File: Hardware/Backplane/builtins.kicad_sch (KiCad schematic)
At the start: 40 parts, among them J1001 Conn_01x06, J1002 Conn_01x06, J1003 Conn_01x06, J1004 Conn_01x06, Q1002 S3134K, Q1004 S3134K, Q1005 S3134K, SW1001 SW_Push, U1003 CD74HC221M96, U1004 PCF8523T/1,118, Y1001 32.768k

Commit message: Adjusts to review comments
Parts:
- removed J1001, J1002, J1003, J1004: Conn_01x06, Connector_PinHeader_2.54mm:PinHeader_1x06_P2.54mm_Vertical, symbol Connector_Generic:Conn_01x06
- removed TP1001, TP1002, TP1003: TestPoint_Small, TestPoint:TestPoint_Pad_D1.0mm, symbol Connector:TestPoint_Small
- added J1001, J1002, J1003, J1005: SM04B-SRSS-TB, symbol Connector_Generic:Conn_01x04
- added R1004, R1006, R1011: 270, Resistor_SMD:R_0603_1608Metric, symbol Device:R
- C1003, C1004: value 1u -> 10u; Digikey Part No (none) -> 1276-1192-1-ND
- R1001, R1002: value 4K7 -> 10K; Digikey Part No (none) -> 311-10.0KHRCT-ND
- R1003, R1009, R1010, R1013, R1016: Digikey Part No (none) -> 311-10.0KHRCT-ND
- R1005, R1007, R1008: footprint (none) -> Resistor_SMD:R_0603_1608Metric; Digikey Part No (none) -> 541-100HCT-ND
- R1014, R1015: value 100K -> 10K; Digikey Part No (none) -> 311-10.0KHRCT-ND
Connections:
- net +3V3: now also R1013.1, J1001.3 (Pin_3), J1002.3 (Pin_3), J1003.3 (Pin_3), J1005.3 (Pin_3)
- net BRD_RESET: now also R1004.2; no longer Q1002.2 (G)
- net GND: now also J1001.4 (Pin_4), J1002.4 (Pin_4), J1003.4 (Pin_4), J1005.4 (Pin_4); no longer R1013.1
- net I2C^{BRD}_{SCL}: now also J1001.1 (Pin_1), J1002.1 (Pin_1), J1003.1 (Pin_1), J1005.1 (Pin_1)
- net I2C^{BRD}_{SDA}: now also J1001.2 (Pin_2), J1002.2 (Pin_2), J1003.2 (Pin_2), J1005.2 (Pin_2)
- net at Q1005.2 (G): now also R1006.1; no longer U1003.13 (1Q)
- net at Q1004.2 (G): now also R1011.1; no longer U1003.5 (2Q)
- new net: Q1002.2 (G), R1004.1
- new net: R1011.2, U1003.5 (2Q)
- new net: R1006.2, U1003.13 (1Q)
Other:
- note removed: "TODO: Change to QWIIC"
- moved on the sheet: Q1005

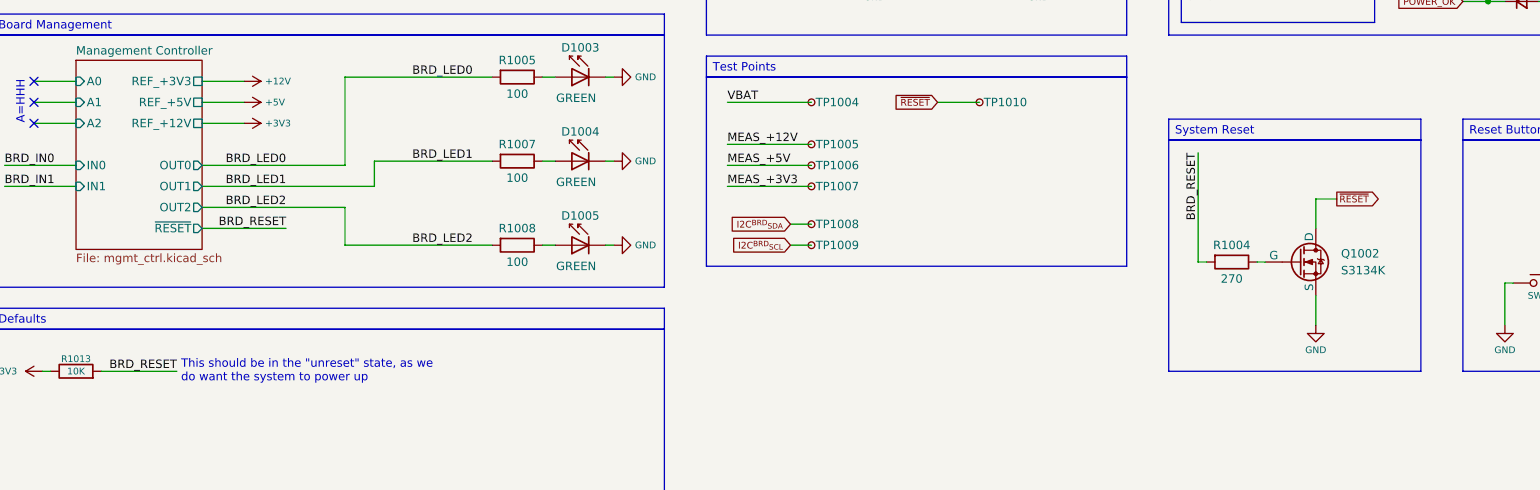
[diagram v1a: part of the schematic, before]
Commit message: Starts refactoring Backplane to use NL17SZS11-D instead of 4-port AND
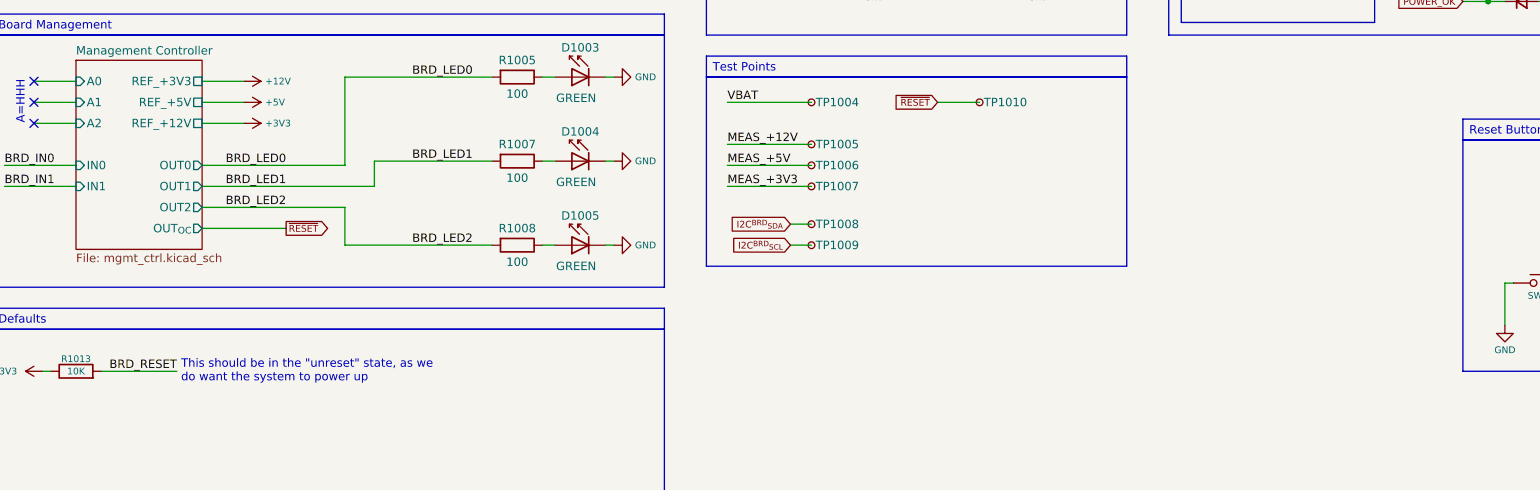
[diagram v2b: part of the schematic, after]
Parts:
- removed Q1002: S3134K, symbol Simulation_SPICE:NMOS
- removed R1004: 270, Resistor_SMD:R_0603_1608Metric, symbol Device:R
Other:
- sheet Management Controller ports: added OUT_{OC}; removed ~{RESET}

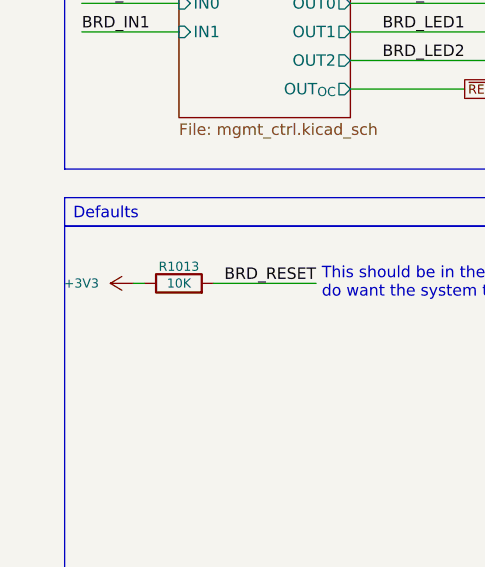
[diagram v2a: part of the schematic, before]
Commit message: Cleans up Backplane schematic even more. Less parts in the BOM, less mistakes!
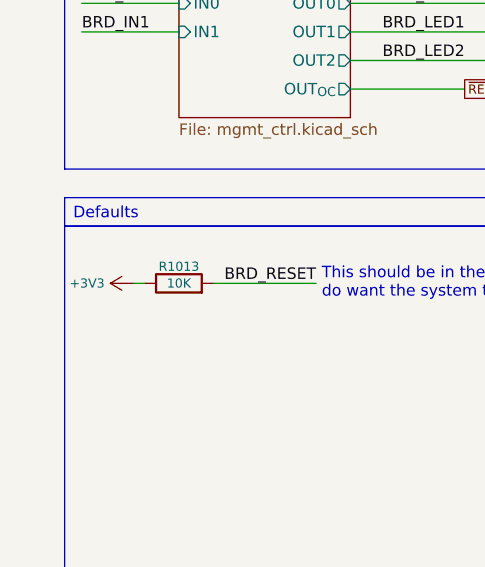
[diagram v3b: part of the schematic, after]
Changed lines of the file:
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@@
 		(on_board yes)
 		(dnp no)
-		(fields_autoplaced yes)
 		(property "Reference" "#PWR01004"
 			(at 30.48 158.75 0)
@@
 		)
 		(property "Value" "+3V3"
-			(at 22.86 158.7499 90)
+			(at 23.495 158.75 90)
 			(effects
 				(font

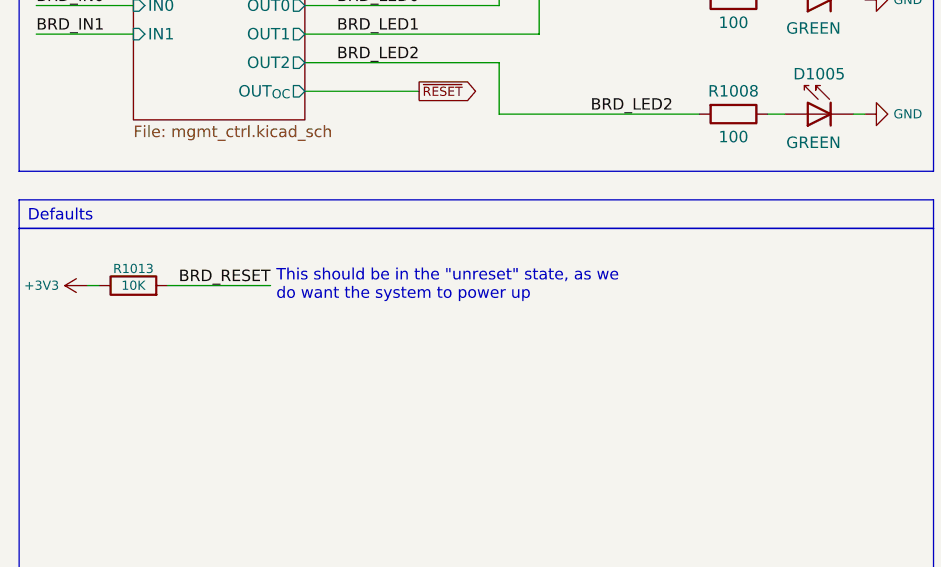
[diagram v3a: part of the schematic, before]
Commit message: Cleans up power connector.
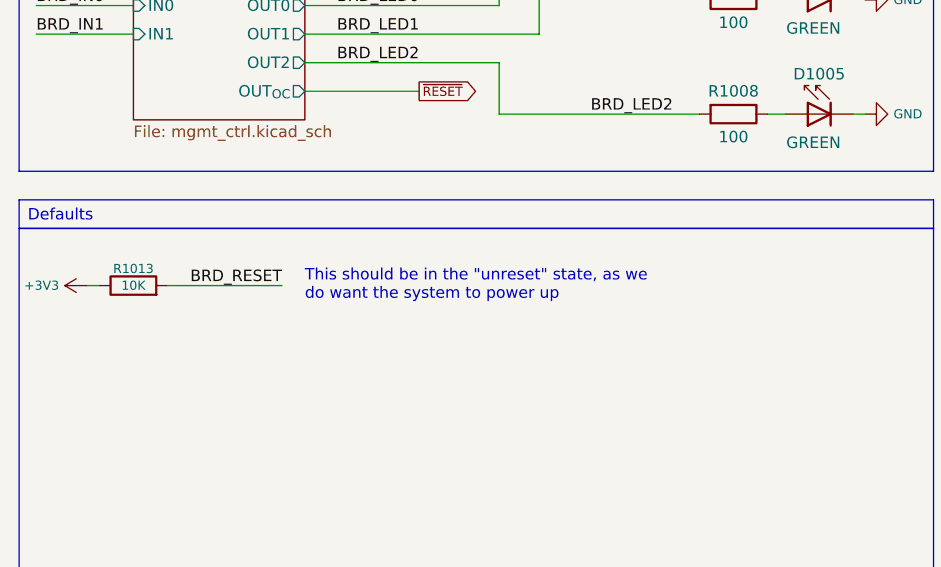
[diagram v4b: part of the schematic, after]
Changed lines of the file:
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@@
 	(text "This should be in the \"unreset\" state, as we\ndo want the system to power up"
 		(exclude_from_sim no)
-		(at 47.625 158.75 0)
+		(at 50.8 158.75 0)
 		(effects
 			(font
@@
 	(wire
 		(pts
-			(xy 35.56 158.75) (xy 46.99 158.75)
+			(xy 35.56 158.75) (xy 48.26 158.75)
 		)
 		(stroke
@@
 	)
 	(label "BRD_RESET"
-		(at 46.99 158.75 180)
-		(effects
-			(font
+		(at 48.26 158.75 180)
+		(effects
+			(font

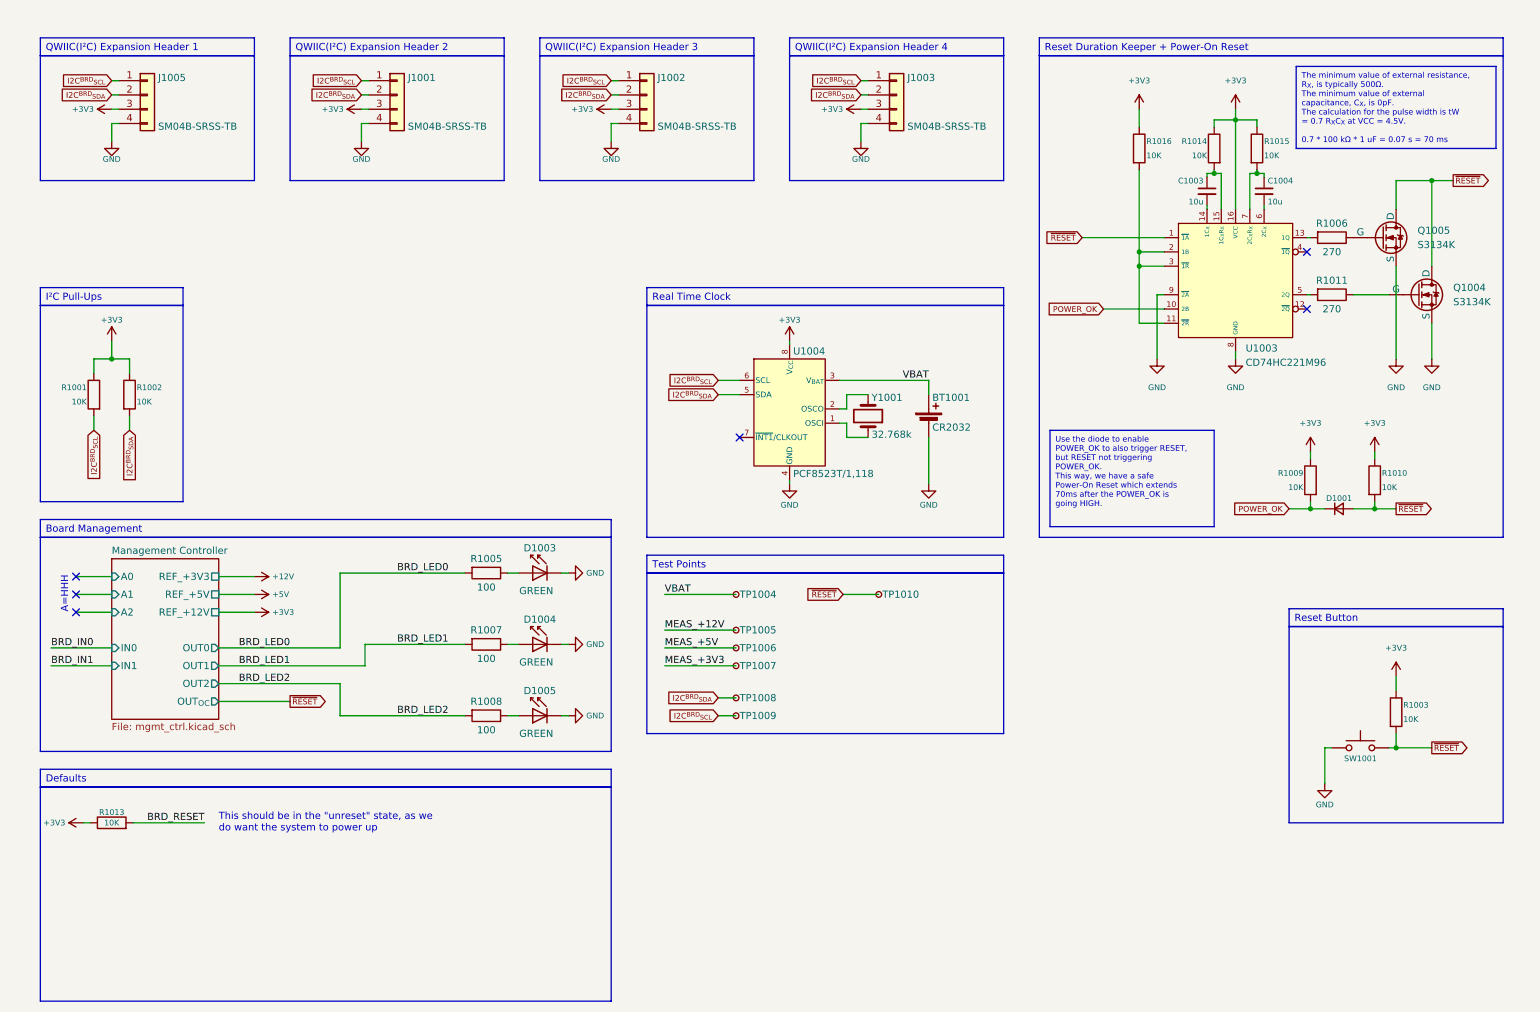
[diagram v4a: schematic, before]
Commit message: Cleans up schematic even more, consolidates 270 and 100 Ohm resistors into the 560 ohm resistor, as they were only used as series resistors for the mosfets and LED current limiters
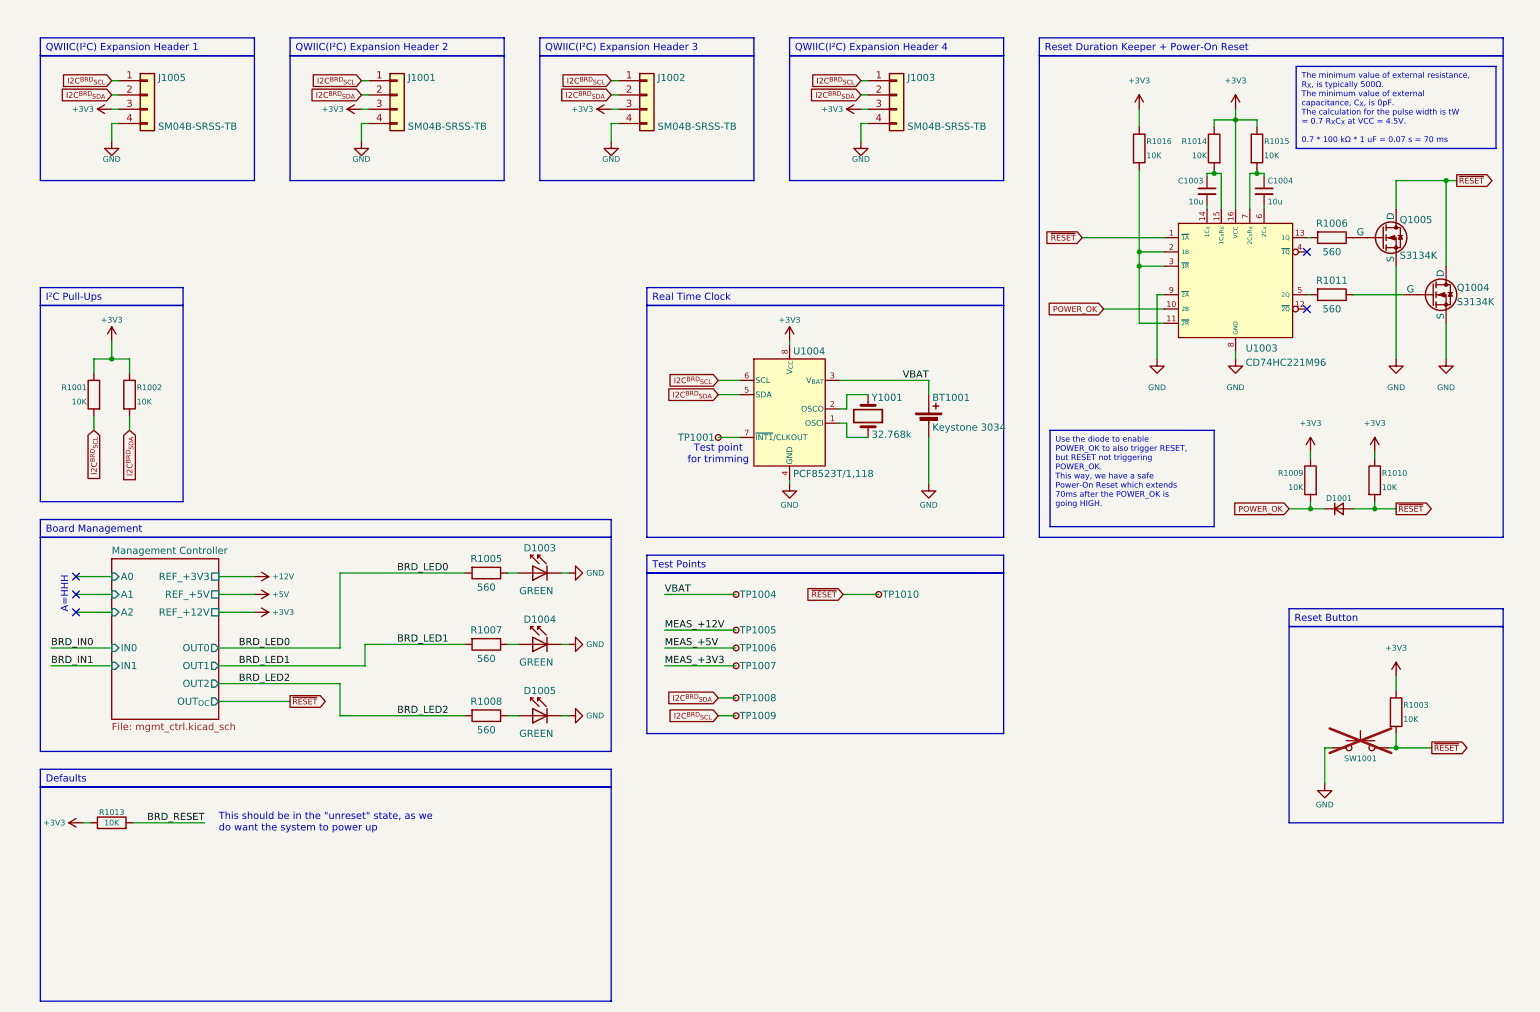
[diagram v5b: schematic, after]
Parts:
- added TP1001: TestPoint_Small, TestPoint:TestPoint_Pad_D1.0mm, symbol Connector:TestPoint_Small
- BT1001: value CR2032 -> Keystone 3034; footprint Battery:Battery_Panasonic_CR2032-HFN_Horizontal_CircularHoles -> Battery:BatteryHolder_Keystone_3034_1x20mm; Digikey Part No (none) -> 36-3034-ND
- Q1004, Q1005: footprint (none) -> Package_TO_SOT_SMD:SOT-23; symbol Simulation_SPICE:NMOS -> Home Computer:S3134K
- R1005, R1007, R1008: value 100 -> 560; Digikey Part No 541-100HCT-ND -> RR08P560DCT-ND
- R1006, R1011: value 270 -> 560; Digikey Part No RMCF0603FT270RCT-ND -> RR08P560DCT-ND
- SW1001: value SW_Push -> Button 12mm; footprint (none) -> Button_Switch_THT:SW_PUSH-12mm; now not fitted
- U1003: footprint (none) -> Package_SO:SOIC-16_3.9x9.9mm_P1.27mm
- Y1001: footprint (none) -> Crystal:Crystal_SMD_3215-2Pin_3.2x1.5mm; Digikey Part No (none) -> 3155-32.768K12.5PI/3215ACT-ND
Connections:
- net GND: now also Q1004.2 (S), Q1005.2 (S); no longer Q1004.3 (S), Q1005.3 (S)
- net ~{RESET}: now also Q1004.3 (D), Q1005.3 (D); no longer Q1004.1 (D), Q1005.1 (D)
- net at R1011.1: now also Q1004.1 (G); no longer Q1004.2 (G)
- net at R1006.1: now also Q1005.1 (G); no longer Q1005.2 (G)
- net at U1004.7 (~{INT1}/CLKOUT): now also TP1001.1
- no-connect marks 6 -> 5
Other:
- note added: "Test point for trimming"
- moved on the sheet: Q1004

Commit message: Further backplane PCB cleanup.
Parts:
- removed J1001, J1002: SM04B-SRSS-TB, symbol Connector_Generic:Conn_01x04
- added J1004, J1006: BM04B-SRSS-TB, Connector_JST:JST_SH_BM04B-SRSS-TB_1x04-1MP_P1.00mm_Vertical, symbol Connector_Generic:Conn_01x04
- J1003, J1005: value SM04B-SRSS-TB -> BM04B-SRSS-TB; footprint (none) -> Connector_JST:JST_SH_BM04B-SRSS-TB_1x04-1MP_P1.00mm_Vertical; Digikey Part No 455-SM04B-SRSS-TBCT-ND -> 455-BM04B-SRSS-TBCT-ND; now not fitted; now left out of the parts list
- SW1001: footprint Button_Switch_THT:SW_PUSH-12mm -> Button_Switch_THT:SW_PUSH_1P1T_6x3.5mm_H4.3_APEM_MJTP1243; Digikey Part No (none) -> 679-2452-ND; now left out of the parts list
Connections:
- net +3V3: now also J1004.3 (Pin_3), J1006.3 (Pin_3)
- net GND: now also J1004.4 (Pin_4), J1006.4 (Pin_4)
- net I2C^{BRD}_{SCL}: now also J1004.1 (Pin_1), J1006.1 (Pin_1)
- net I2C^{BRD}_{SDA}: now also J1004.2 (Pin_2), J1006.2 (Pin_2)
